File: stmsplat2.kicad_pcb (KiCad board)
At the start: 2 copper layers, 71.1 x 124.2 mm, 97 parts, among them J1 C11_2X36, J10 Conn_01x03_Male, J11 Conn_01x02_Male, J12 Conn_01x04_Male, J13 Conn_01x04_Male, J14 Conn_01x02, J15 Conn_01x02, J16 Screw_Terminal_01x03, J17 Screw_Terminal_01x02, J2 C12_2X36, J3 Conn_01x04_Male, J4 Conn_01x04_Male, J5 Conn_Coaxial, J6 Conn_01x06, J7 Conn_01x04_Male, J8 Conn_01x04_Male, J9 Conn_01x03_Male, Q1 BSS138LT1G, U1 ublox_chinese_PCB_module, U10 XCVR_E30-400M20S, U2 ESP32-C3-13, U3 SST25VF032B, U4 48L512-48LM01, U5 Opamp_Quad_MCP6024, U6 E180-ZG120A, U7 AZ1084C, U8 MCP6S93-X_UN, U9 DS2485

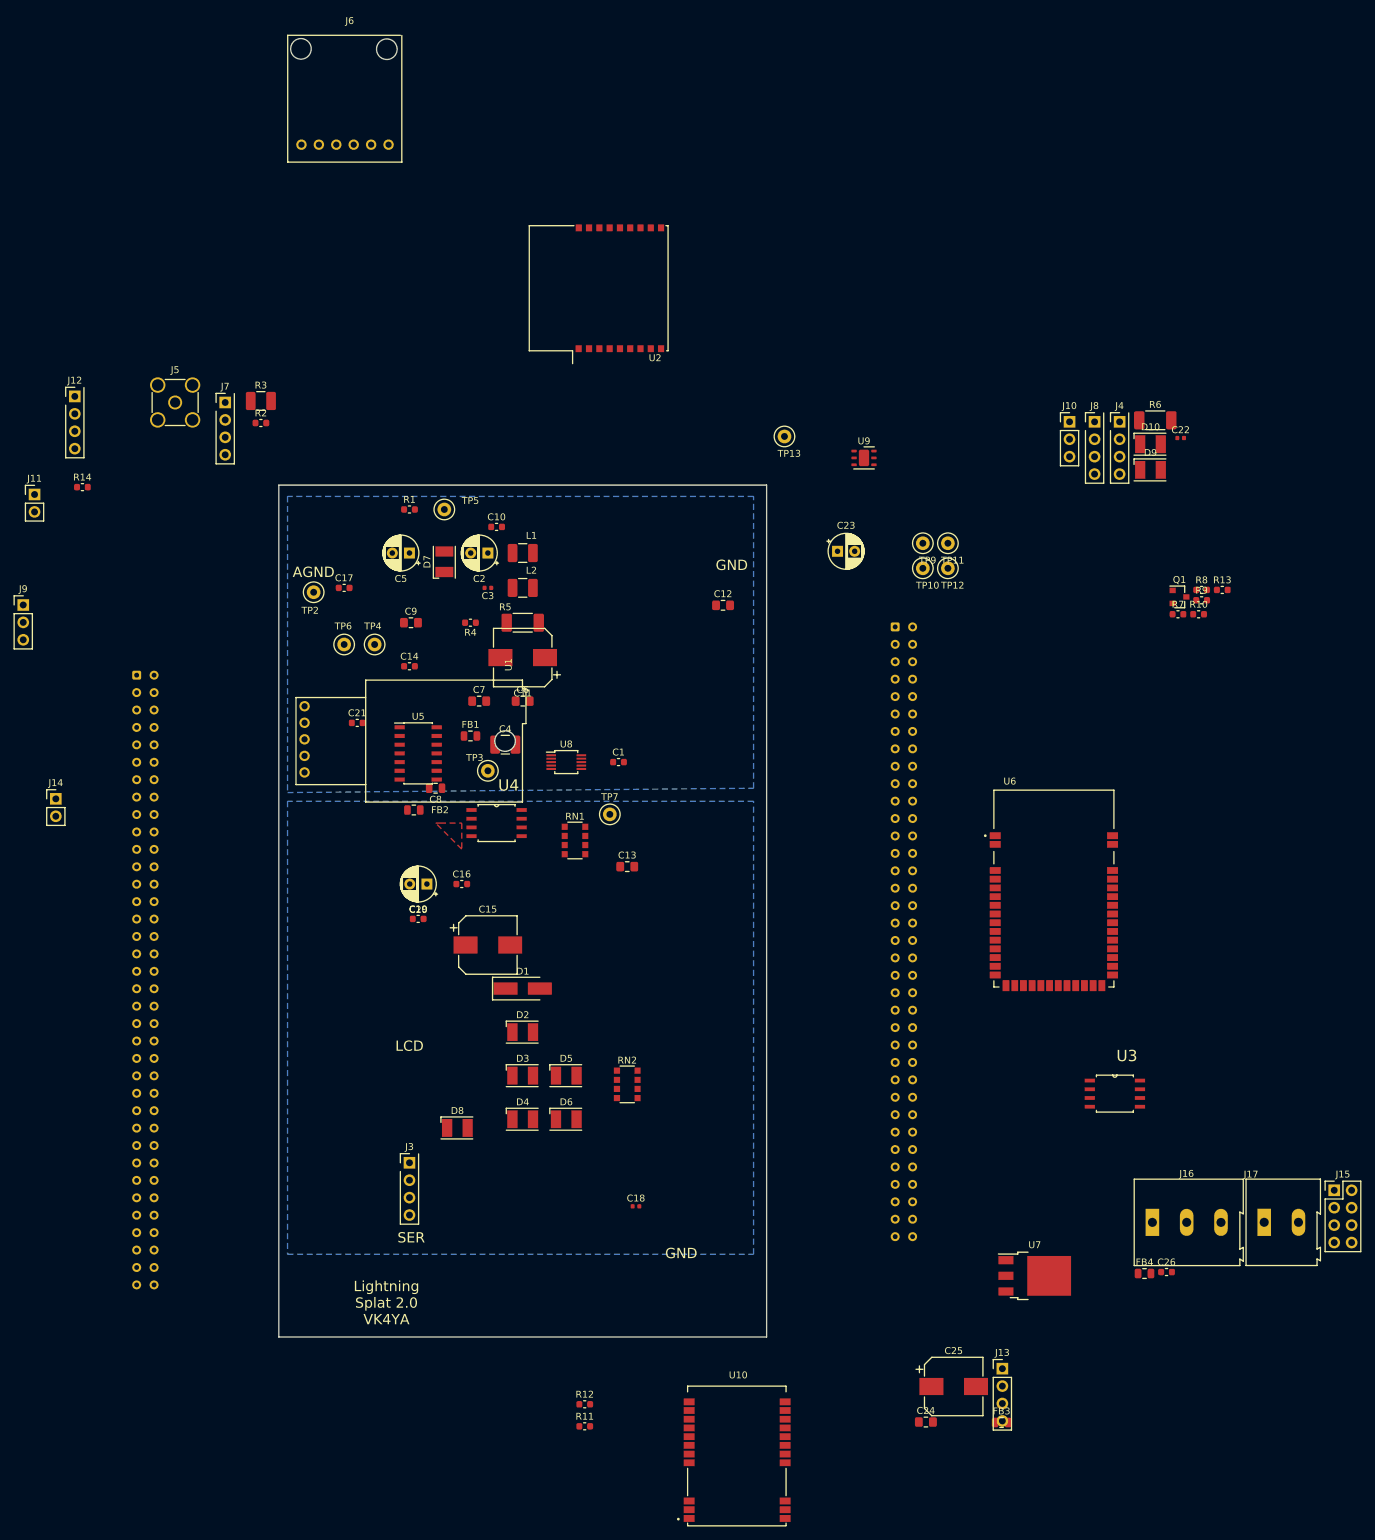
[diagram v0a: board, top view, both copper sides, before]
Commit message: changed all 0603 footprints to 0805 in the schematic
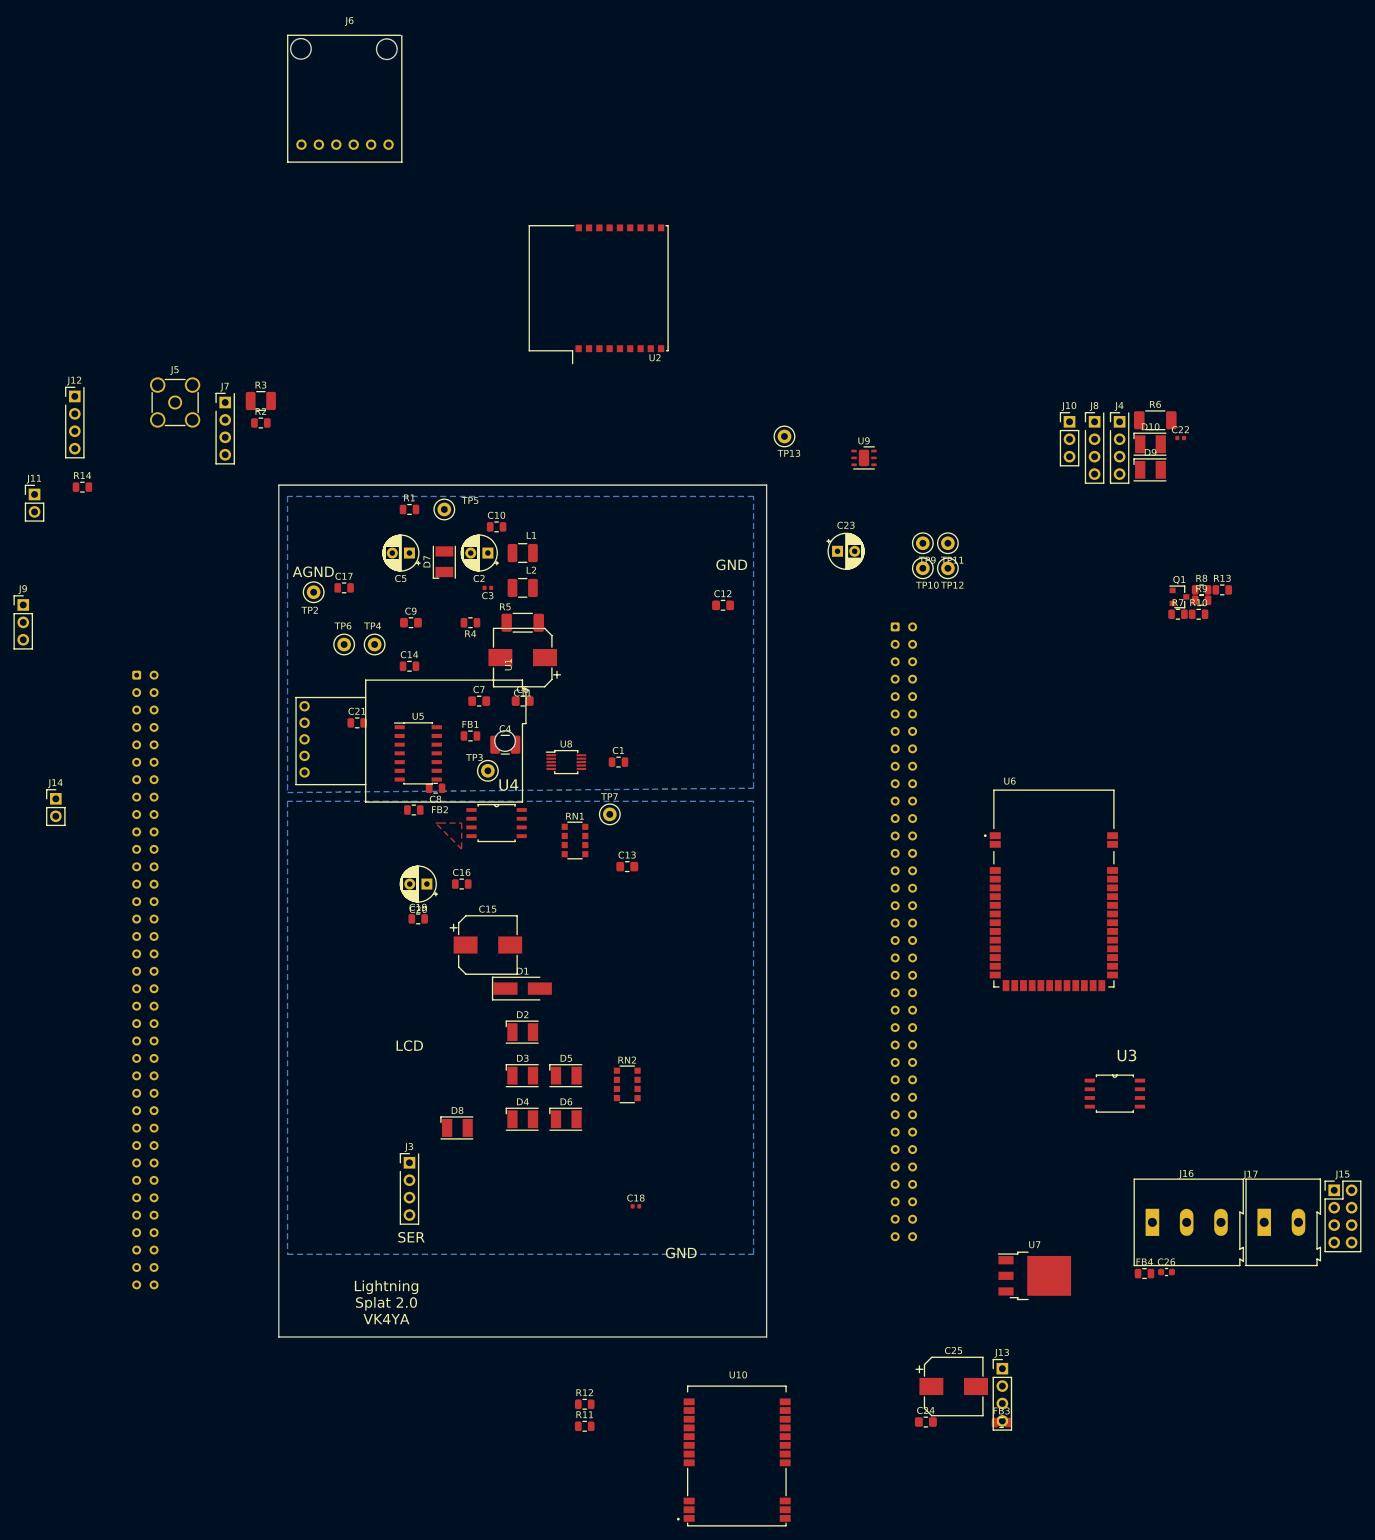
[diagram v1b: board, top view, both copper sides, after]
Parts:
- C1, C10, C14, C16, C17, C19, C21: footprint Capacitor_SMD:C_0603_1608Metric -> Capacitor_SMD:C_0805_2012Metric
- R1, R10, R11, R12, R13, R14, R2, R4, R7, R8, R9: footprint Resistor_SMD:R_0603_1608Metric -> Resistor_SMD:R_0805_2012Metric

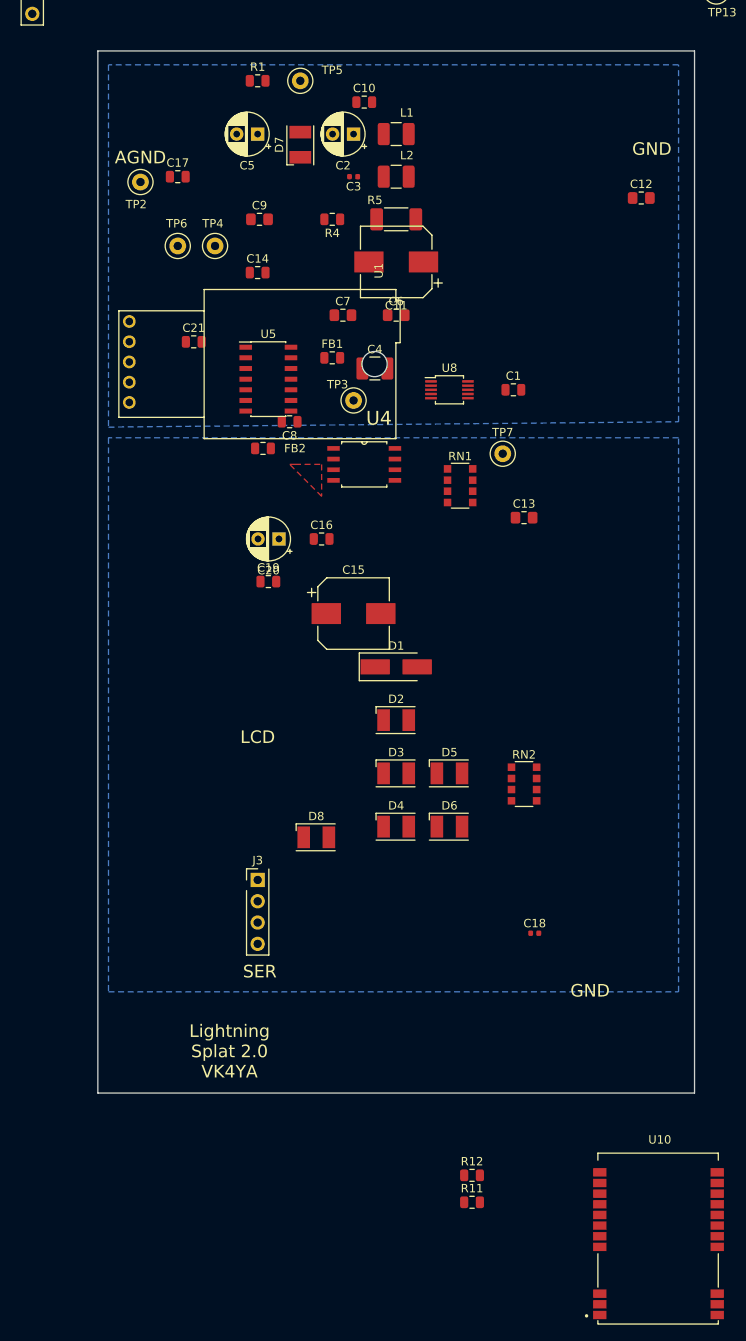
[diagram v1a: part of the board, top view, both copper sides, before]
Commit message: deleted old splat1 pcb outline
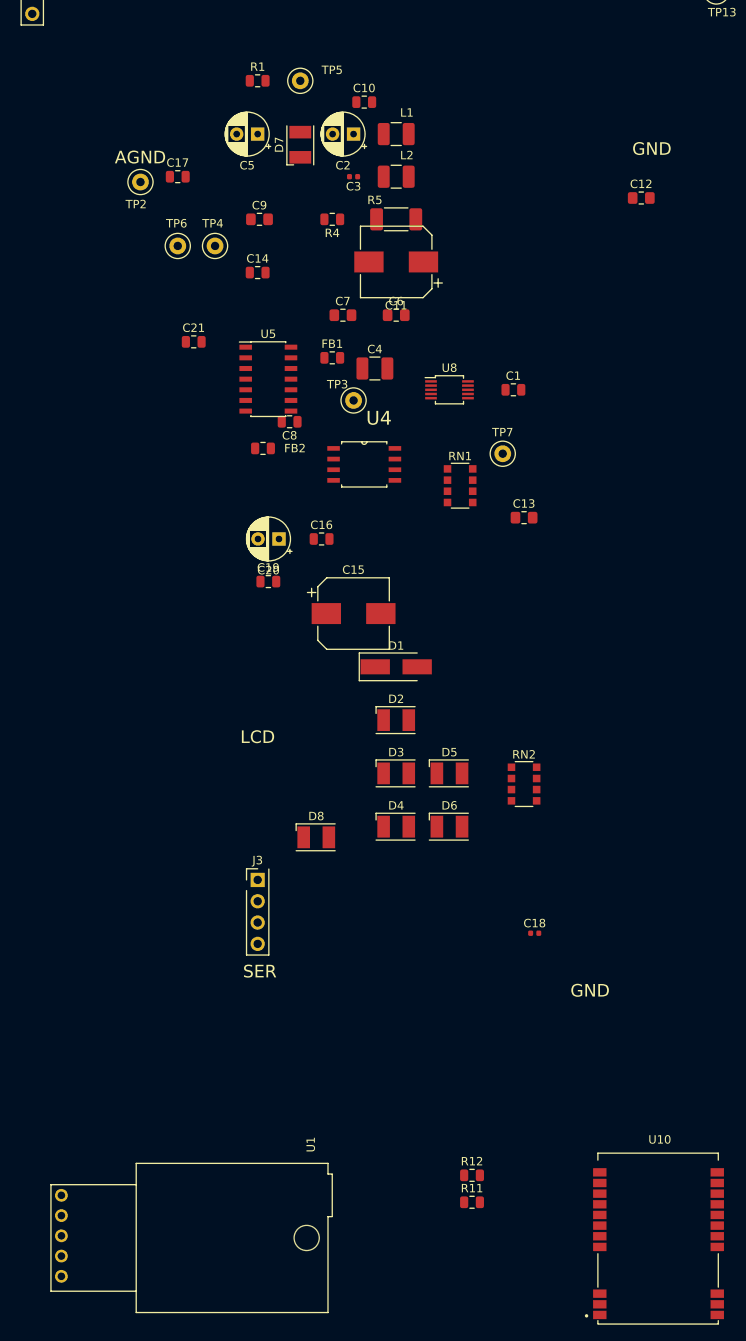
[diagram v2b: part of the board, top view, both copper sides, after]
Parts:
- moved U1 104.5 mm to (50.3, 169.7)
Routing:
- removed copper zone on F.Cu, net /A3V3
- removed copper zone on B.Cu, net GND
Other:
- board outline removed
- board text removed: "Lightning Splat 2.0 VK4YA"

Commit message: Removed more spatboard references
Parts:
- J12, J3, J4, J7, J8: footprint spatboard:PinHeader_1x04_P2.54mm_Vertical -> PinHeader_1x04_P2.54mm_Vertical
- U1: footprint spatboard:NEO7_GPS_MODULE -> NEO7_GPS_MODULE
- U10: footprint spatboard:XCVR_E30-400M20S -> XCVR_E30-400M20S
- U2: footprint spatboard:ESP-C3-13 -> ESP-C3-13
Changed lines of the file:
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@@
     )
   )
-  (module spatboard:ESP-C3-13 (layer F.Cu)
+  (module ESP-C3-13 (layer F.Cu)
     (at 104.3432 4.572 90)
     (descr http://espressif.com/sites/default/files/documentation/0c-esp-wroom-02_datasheet_en.pdf)
@@
     )
   )
-  (module spatboard:NEO7_GPS_MODULE locked (layer F.Cu)
+  (module NEO7_GPS_MODULE locked (layer F.Cu)
     (at 50.292 169.672)
     (descr "Connector IDC Locked, 10 contacts, compatible header: PANCON HE10 (Series 50, (https://www.reboul.fr/storage/00003af6.pdf)")
@@
     )
   )
-  (module spatboard:PinHeader_1x04_P2.54mm_Vertical (layer F.Cu)
+  (module PinHeader_1x04_P2.54mm_Vertical (layer F.Cu)
     (at 24.8666 20.3454)
     (descr "Through hole straight pin header, 1x04, 2.54mm pitch, single row")
@@
     )
   )
-  (module spatboard:XCVR_E30-400M20S (layer F.Cu)
+  (module XCVR_E30-400M20S (layer F.Cu)
     (at 121.3866 164.846)
     (fp_text reference U10 (at 0.2032 -1.8034) (layer F.SilkS)
@@
     )
   )
-  (module spatboard:PinHeader_1x04_P2.54mm_Vertical (layer F.Cu)
+  (module PinHeader_1x04_P2.54mm_Vertical (layer F.Cu)
     (at 73.66 132.08)
     (descr "Through hole straight pin header, 1x04, 2.54mm pitch, single row")
@@
     )
   )
-  (module spatboard:PinHeader_1x04_P2.54mm_Vertical (layer F.Cu)
+  (module PinHeader_1x04_P2.54mm_Vertical (layer F.Cu)
     (at 177.196801 24.050001)
     (descr "Through hole straight pin header, 1x04, 2.54mm pitch, single row")
@@
     )
   )
-  (module spatboard:PinHeader_1x04_P2.54mm_Vertical (layer F.Cu)
+  (module PinHeader_1x04_P2.54mm_Vertical (layer F.Cu)
     (at 173.546801 24.050001)
     (descr "Through hole straight pin header, 1x04, 2.54mm pitch, single row")
@@
     )
   )
-  (module spatboard:PinHeader_1x04_P2.54mm_Vertical (layer F.Cu)
+  (module PinHeader_1x04_P2.54mm_Vertical (layer F.Cu)
     (at 46.793201 21.230601)
     (descr "Through hole straight pin header, 1x04, 2.54mm pitch, single row")
